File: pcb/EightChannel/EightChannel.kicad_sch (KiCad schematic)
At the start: 11 parts, among them J101 UDP, J102 Barrel_Jack_Switch, J103 Conn_01x04_Female, J104 Conn_01x07_Female, U101 74LS595

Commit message: Schematic updates
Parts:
- removed J103: Conn_01x04_Female, Connector_PinSocket_2.54mm:PinSocket_1x04_P2.54mm_Vertical, symbol Connector:Conn_01x04_Female
- added J?: Conn_01x07_Female, symbol Connector:Conn_01x07_Female
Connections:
- net VDD is gone; now on net PA0_PDI: C101.1, C?.1, D101.2 (A), J101.2 (Pin_2), R101.1, U101.10 (~{SRCLR}), U101.16 (VCC), U?.1 (VCC)
- net GND: now also J?.7 (Pin_7)
- net PA5: now also J104.3 (Pin_3); no longer J104.5 (Pin_5)
- net PA6: now also J104.4 (Pin_4); no longer J104.6 (Pin_6)
- net PA7: now also J104.5 (Pin_5); no longer J104.7 (Pin_7)
- net PB0: now also J?.2 (Pin_2)
- net PB1: now also J?.1 (Pin_1)
- net PB2_TxD: now also J104.7 (Pin_7)
- net PB3_RxD: now also J104.6 (Pin_6)
- net CLK_PIN renamed PA2_CLK
- net PA2_CLK: now also J?.5 (Pin_5); no longer J104.2 (Pin_2)
- net DATA_PIN renamed PA1_DATA
- net PA1_DATA: now also J?.4 (Pin_4); no longer J104.3 (Pin_3)
- net LATCH_PIN renamed PA3_LATCH
- net PA3_LATCH: now also J?.6 (Pin_6); no longer J104.1 (Pin_1)
- net PA0 renamed PA0_PDI
- net PA0_PDI: now also J104.1 (Pin_1), J?.3 (Pin_3)
- net ~{ENABLE} renamed PA4_~{ENABLE}
- net PA4_~{ENABLE}: now also J104.2 (Pin_2); no longer J104.4 (Pin_4)
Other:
- moved on the sheet: C102, R101, U?

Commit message: Intermediate
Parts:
- added H101, H102, H103, H104: MountingHole, MountingHole:MountingHole_2.5mm, symbol Mechanical:MountingHole
- added JP101: Ext, Jumper:SolderJumper-2_P1.3mm_Bridged_RoundedPad1.0x1.5mm, symbol Jumper:SolderJumper_2_Bridged
- added M101: NODEMCU_ESP8266, advent_sternla:NODEMCU_ESP8266, symbol advent_sternla_attiny1614_symbols:NODEMCU_ESP8266
- J104: renamed from J?; footprint (none) -> Connector_PinSocket_2.54mm:PinSocket_1x07_P2.54mm_Vertical
- gave numbers to parts that had none: 2
- renumbered C102 to C103, J102 to J101, J101 to J102, J104 to J103, U101 to U102
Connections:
- net GND: now also M101.2 (GND), M101.25 (GND), M101.29 (GND), M101.9 (GND)
- net PA0_PDI: no longer C101.1, C102.1, D101.2 (A), J102.2 (Pin_2), J103.1 (Pin_1), R101.1, U101.1 (VCC), U102.10 (~{SRCLR}), U102.16 (VCC)
- net PB2_TxD: now also M101.4 (GPIO3_RxD0)
- net PB3_RxD: now also M101.3 (GPIO1_TxD0)
- new net: JP101.1 (A), M101.30 (VIN)
- new net VDD: C101.1, C102.1, D101.2 (A), J102.2 (Pin_2), J103.1 (Pin_1), JP101.2 (B), R101.1, U101.1 (VCC), U102.10 (~{SRCLR}), U102.16 (VCC)
- no-connect marks 5 -> 28
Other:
- moved on the sheet: J102

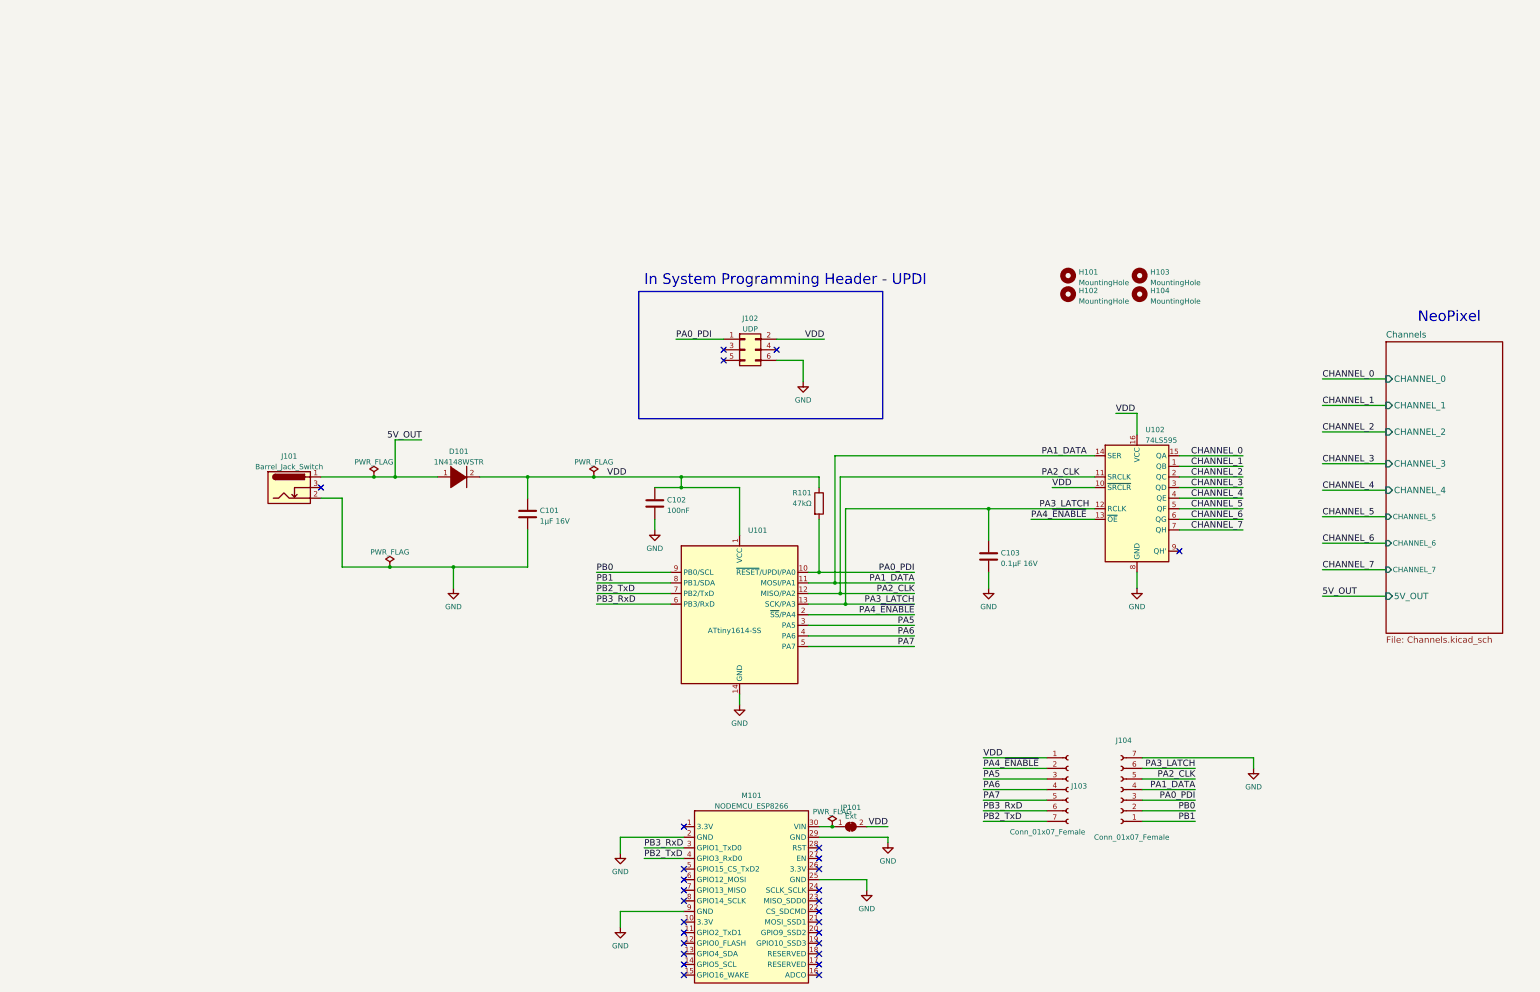
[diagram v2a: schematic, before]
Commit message: Finished 8Channel and submitted to Fab
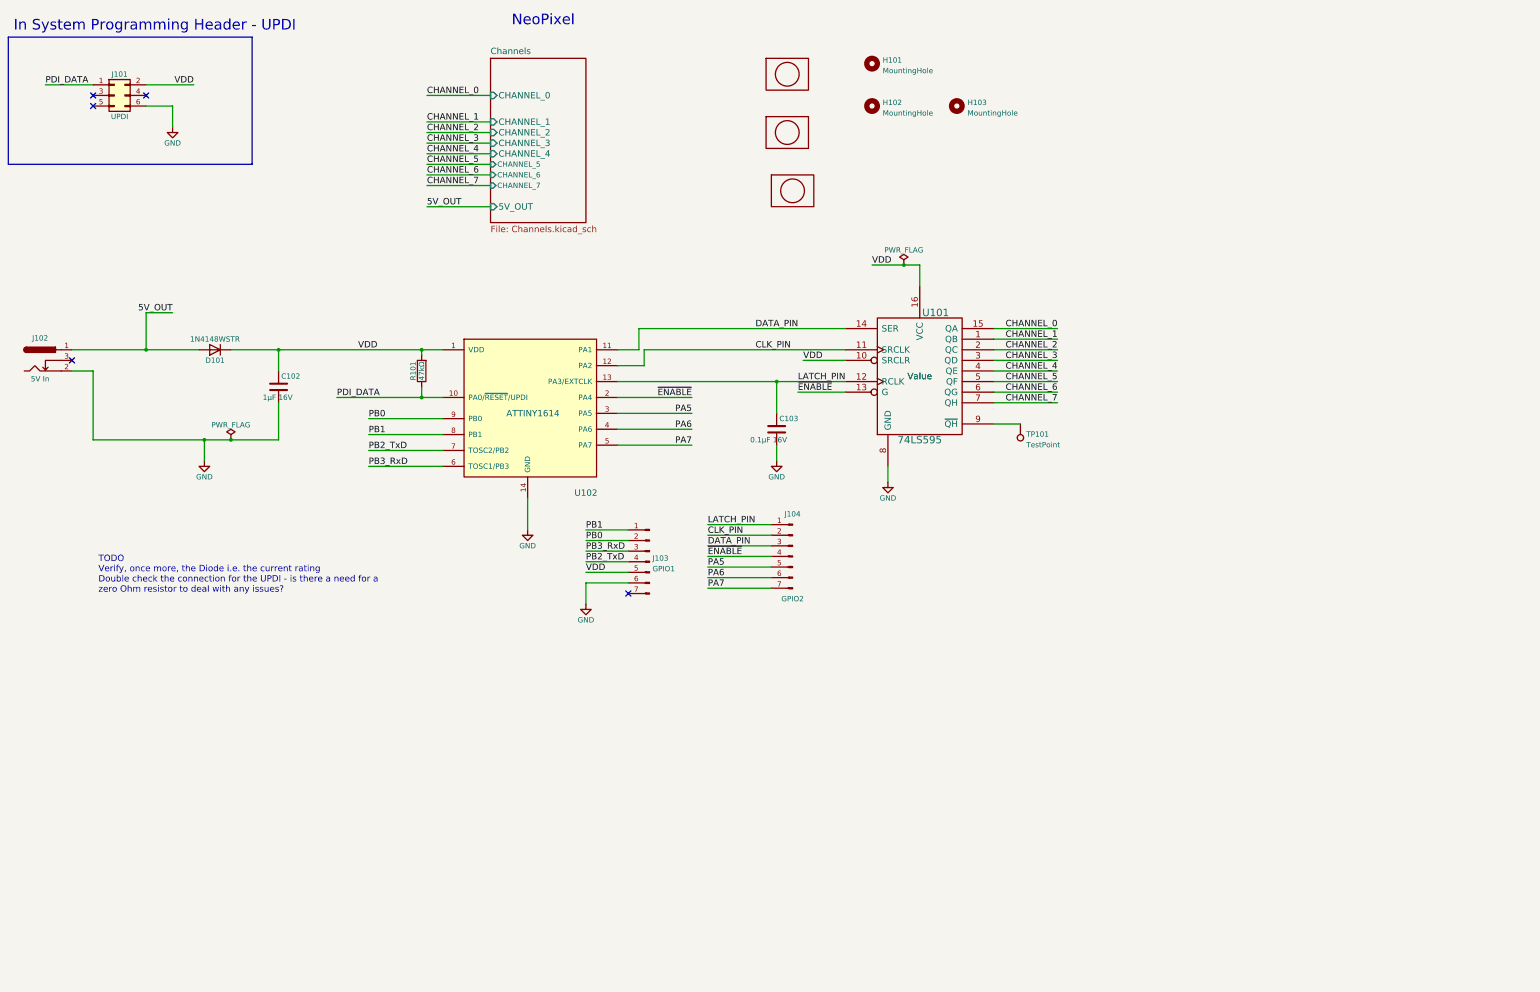
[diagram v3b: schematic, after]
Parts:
- removed C101: 1μF 16V, Capacitor_SMD:C_0805_2012Metric, symbol Device:C
- removed C102: 100nF, Capacitor_SMD:C_0805_2012Metric, symbol Device:C
- removed C103: 0.1μF 16V, Capacitor_SMD:C_0805_2012Metric, symbol Device:C
- removed D101: 1N4148WSTR, Diode_SMD:D_SOD-123F, symbol pspice:DIODE
- removed H104: MountingHole, MountingHole:MountingHole_2.5mm, symbol Mechanical:MountingHole
- removed J101: Barrel_Jack_Switch, advent_sternla:CONN_PWR_JACK_1_3X3_5MM_SOLDER, symbol Connector:Barrel_Jack_Switch
- removed J102: UDP, advent_sternla:TC2030-IDC-FP_ISP_Connector, symbol Connector_Generic:Conn_02x03_Odd_Even
- removed J103, J104: Conn_01x07_Female, Connector_PinSocket_2.54mm:PinSocket_1x07_P2.54mm_Vertical, symbol Connector:Conn_01x07_Female
- removed JP101: Ext, Jumper:SolderJumper-2_P1.3mm_Bridged_RoundedPad1.0x1.5mm, symbol Jumper:SolderJumper_2_Bridged
- removed M101: NODEMCU_ESP8266, advent_sternla:NODEMCU_ESP8266, symbol advent_sternla_attiny1614_symbols:NODEMCU_ESP8266
- removed R101: 47kΩ, Resistor_SMD:R_0805_2012Metric, symbol Device:R
- removed U101: ATtiny1614-SS, Package_SO:SOIC-14_3.9x8.7mm_P1.27mm, symbol NEO_EightChannel:ATtiny1614-SS
- removed U102: 74LS595, Package_SO:SOIC-16_3.9x9.9mm_P1.27mm, symbol 74xx:74LS595
- added C102: 1μF 16V, Capacitors_SMD:C_0805_HandSoldering, symbol EightChannel-rescue:C
- added C103: 0.1μF 16V, Capacitors_SMD:C_0805_HandSoldering, symbol EightChannel-rescue:C
- added D101: 1N4148WSTR, Diodes_SMD:D_SOD-123F, symbol EightChannel-rescue:D
- added J101: UPDI, advent_sternla:PRG_TC2030-IDC-NL, symbol EightChannel-rescue:Conn_02x03_Odd_Even
- added J102: 5V In, advent_sternla:CONN_PWR_JACK_1_3X3_5MM_SOLDER, symbol EightChannel-rescue:Jack-DC
- added J103: GPIO1, Connector_PinHeader_2.54mm:PinHeader_1x07_P2.54mm_Vertical, symbol Connector:Conn_01x07_Male
- added J104: GPIO2, Connector_PinHeader_2.54mm:PinHeader_1x07_P2.54mm_Vertical, symbol EightChannel-rescue:Conn_01x07_Male
- added Lg101: logo, mech:MyBasic_rounded_50_1, symbol mech:logo
- added Lg102: logo, Symbol:KiCad-Logo2_5mm_SilkScreen, symbol mech:logo
- added Lg103: logo, advent_sternla:QR_AdventSternla_FS, symbol mech:logo
- added R101: 47kΩ, Resistor_SMD:R_0805_2012Metric, symbol EightChannel-rescue:R
- added TP101: TestPoint, TestPoint:TestPoint_THTPad_D1.0mm_Drill0.5mm, symbol Connector:TestPoint
- added U101: 74LS595, Housings_SOIC:SOIC-16_3.9x9.9mm_Pitch1.27mm, symbol EightChannel-rescue:74LS596-RESCUE-EightChannel
- added U102: ATTINY1614, Package_SO:SOIC-14_3.9x8.7mm_P1.27mm, symbol EightChannel-rescue:ATTINY1614
- H101, H102, H103: footprint MountingHole:MountingHole_2.5mm -> MountingHole:MountingHole_2.7mm_M2.5
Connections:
- net 5V_OUT: now also D101.2 (A), J102.1
- net CHANNEL_0: now also U101.15 (QA)
- net CHANNEL_1: now also U101.1 (QB)
- net CHANNEL_2: now also U101.2 (QC)
- net CHANNEL_3: now also U101.3 (QD)
- net CHANNEL_4: now also U101.4 (QE)
- net CHANNEL_5: now also U101.5 (QF)
- net CHANNEL_6: now also U101.6 (QG)
- net CHANNEL_7: now also U101.7 (QH)
- net GND: now also C102.2, C103.2, J101.6 (Pin_6), J102.2, J103.6 (Pin_6), U101.8 (GND), U102.14 (GND)
- net PA5: now also J104.5 (Pin_5), U102.3 (PA5)
- net PA6: now also J104.6 (Pin_6), U102.4 (PA6)
- net PA7: now also J104.7 (Pin_7), U102.5 (PA7)
- net PB0: now also J103.2 (Pin_2), U102.9 (PB0)
- net PB1: now also J103.1 (Pin_1), U102.8 (PB1)
- net PB2_TxD: now also J103.4 (Pin_4), U102.7 (TOSC2/PB2)
- net PB3_RxD: now also J103.3 (Pin_3), U102.6 (TOSC1/PB3)
- net VDD: now also C102.1, D101.1 (K), J101.2 (Pin_2), J103.5 (Pin_5), R101.2, U101.10 (SRCLR), U101.16 (VCC), U102.1 (VDD)
- new net: TP101.1, U101.9 (~{QH})
- new net CLK_PIN: J104.2 (Pin_2), U101.11 (SRCLK), U102.12 (PA2)
- new net DATA_PIN: J104.3 (Pin_3), U101.14 (SER), U102.11 (PA1)
- new net LATCH_PIN: C103.1, J104.1 (Pin_1), U101.12 (RCLK), U102.13 (PA3/EXTCLK)
- new net PDI_DATA: J101.1 (Pin_1), R101.1, U102.10 (PA0/~{RESET}/UPDI)
- new net ~{ENABLE}: J104.4 (Pin_4), U101.13 (G), U102.2 (PA4)
- no-connect marks 28 -> 5
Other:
- note added: "TODO Verify, once more, the Diode i.e. the current rating Double check the connection for the UPDI - is there a need for a zero Ohm resistor to deal with any issues?"
- company: (none) -> SM
- title: (none) -> Advent Sternal - NeoPixel Driver

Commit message: Update and synch of the eight channel design
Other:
- note removed: "TODO Verify, once more, the Diode i.e. the current rating Double check the connection for the UPDI - is there a need for a zero Ohm resistor to deal with any issues?"
- moved on the sheet: C102, C103, D101, J102, J103, J104, R101, TP101, U101, U102
